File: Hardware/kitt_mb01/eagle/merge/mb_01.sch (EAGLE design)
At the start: 119 parts, among them IC1.01 RT8293A, IC2.00 BQ24266RGET, IC3.01 LSM9DS1, U0.1 SI1922EDH, U6.01 TPS61032RSARPSDO-G16, U7.01 SI1922EDH, U7.2 SI1922EDH, X2.01 S2B-PH-K-S(LF)(SN), X7.02 ARDUINO_UNO, X7.03 CON_HEADER_1X02, X7.05 MOTOR, X7.06 CON_HEADER_1X02, X7.08 CON_HEADER_1X02, X7.09 0R-JUMPA, X7.10 0R-JUMPA, X7.11 CON_HEADER_1X02

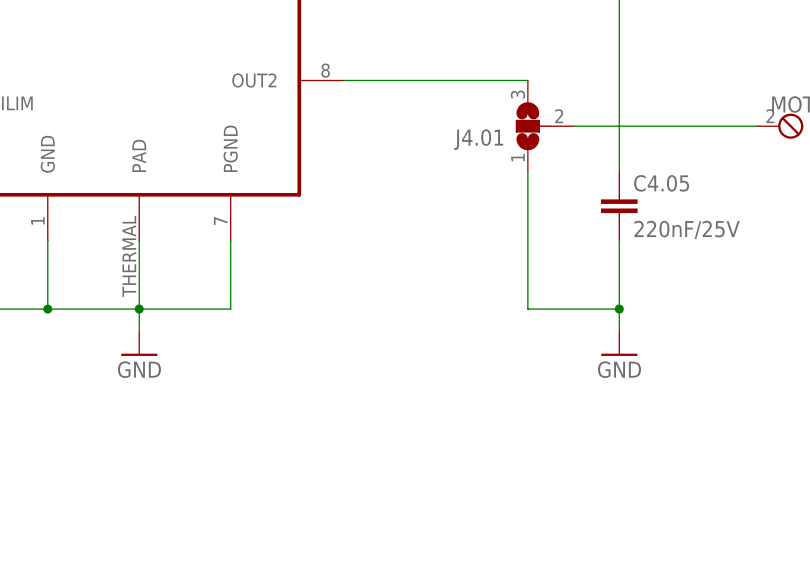
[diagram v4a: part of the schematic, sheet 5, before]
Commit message: updated bill of materials, changed some footprints
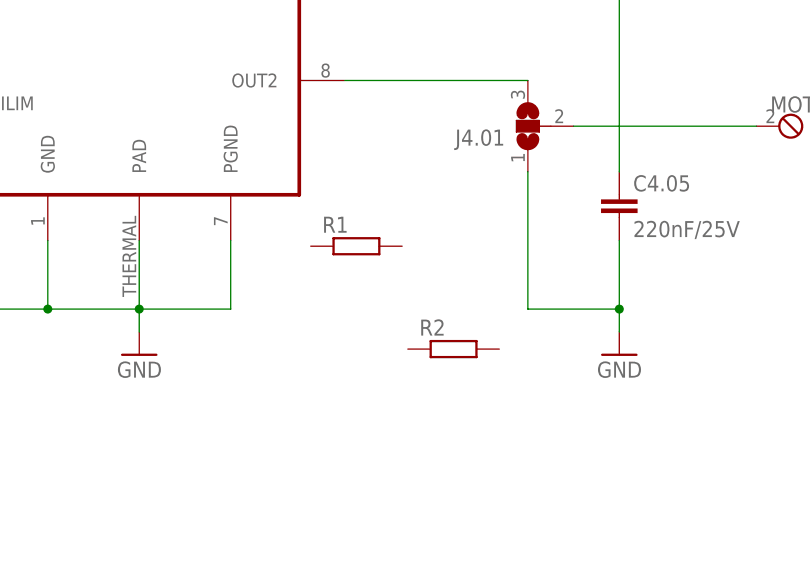
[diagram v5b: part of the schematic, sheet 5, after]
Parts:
- added R1: (no value), rcl:R-EU_R0805
- added R2: (no value), rcl:R-EU_R0402
- F1.01: device rcl:R-EU_R0805 -> rcl:R-EU_R1210
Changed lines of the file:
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@@
 <part name="P+6" library="supply1" deviceset="+12V" device="" value="V.POW"/>
 <part name="D1.01" library="diode" deviceset="MBRS3*0T3" device="" technology="2"/>
-<part name="F1.01" library="rcl" deviceset="R-EU_" device="R0805" value="750mA"/>
+<part name="F1.01" library="rcl" deviceset="R-EU_" device="R1210" value="750mA"/>
 <part name="L1.01" library="inductors" deviceset="BLM15H" device="" technology="B121SN1" value="BEAD"/>
 <part name="P+2" library="supply1" deviceset="+12V" device="" value="V.POW"/>
@@
 <part name="X7.03" library="kitt.con" deviceset="CON_HEADER_1X02" device=""/>
 <part name="R7.10" library="rcl" deviceset="R-EU_" device="R1206" value="330R"/>
+<part name="R1" library="rcl" deviceset="R-EU_" device="R0805"/>
+<part name="R2" library="rcl" deviceset="R-EU_" device="R0402"/>
 </parts>
 <sheets>
@@
 <instance part="R4.05" gate="G$1" x="99.06" y="73.66" rot="R90"/>
 <instance part="J4.01" gate="G$1" x="193.04" y="81.28" rot="R180"/>
+<instance part="R1" gate="G$1" x="173.99" y="67.945"/>
+<instance part="R2" gate="G$1" x="184.785" y="56.515"/>
 </instances>
 <busses>

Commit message: swapped footprint of LED resistors from 1206 to 0402
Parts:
- R7.04, R7.08, R7.09, R7.10: device rcl:R-EU_R1206 -> rcl:R-EU_R0603
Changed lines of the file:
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@@
 <part name="P+5VMAIN4" library="supply1" deviceset="+5V" device="" value="+5V-MAIN"/>
 <part name="U7.01" library="kitt.ic" deviceset="SI1922EDH" device=""/>
-<part name="R7.04" library="rcl" deviceset="R-EU_" device="R1206" value="330R"/>
+<part name="R7.04" library="rcl" deviceset="R-EU_" device="R0603" value="330R"/>
 <part name="GND33" library="supply1" deviceset="GND" device=""/>
 <part name="X7.10" library="jump-0r-smd" deviceset="0R-JUMP" device="A"/>
@@
 <part name="+3V10" library="supply1" deviceset="+3V3" device=""/>
 <part name="U7.2" library="kitt.ic" deviceset="SI1922EDH" device=""/>
-<part name="R7.09" library="rcl" deviceset="R-EU_" device="R1206" value="[0R]"/>
+<part name="R7.09" library="rcl" deviceset="R-EU_" device="R0603" value="[0R]"/>
 <part name="GND34" library="supply1" deviceset="GND" device=""/>
 <part name="X7.09" library="jump-0r-smd" deviceset="0R-JUMP" device="A"/>
@@
 <part name="X7.08" library="kitt.con" deviceset="CON_HEADER_1X02" device=""/>
 <part name="X7.11" library="kitt.con" deviceset="CON_HEADER_1X02" device=""/>
-<part name="R7.08" library="rcl" deviceset="R-EU_" device="R1206" value="330R"/>
+<part name="R7.08" library="rcl" deviceset="R-EU_" device="R0603" value="330R"/>
 <part name="GND12" library="supply1" deviceset="GND" device=""/>
 <part name="X7.06" library="kitt.con" deviceset="CON_HEADER_1X02" device=""/>
 <part name="X7.03" library="kitt.con" deviceset="CON_HEADER_1X02" device=""/>
-<part name="R7.10" library="rcl" deviceset="R-EU_" device="R1206" value="330R"/>
+<part name="R7.10" library="rcl" deviceset="R-EU_" device="R0603" value="330R"/>
 <part name="R1" library="rcl" deviceset="R-EU_" device="R0805"/>
 <part name="R2" library="rcl" deviceset="R-EU_" device="R0402"/>

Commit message: changed yet more footprints -> mainly the beads, stepped it up to a beefier part,    can handle 6A, should be better than the previous 1A rating
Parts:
- removed L1.01, L1.03, L4.01: BEAD, inductors:BLM15HB121SN1
- removed R1: (no value), rcl:R-EU_R0805
- removed R2: (no value), rcl:R-EU_R0402
- added FB1.01, FB1.02, FB4.01: BEAD, rcl:L-EUL4516C
- added L1: (no value), rcl:L-EUL1812
- added L2: (no value), rcl:L-EUL4516C
- C3.01: device rcl:C-EUC0402 -> rcl:C-EUC0603
- FB6.01: device inductors:BLM15HB121SN1 -> rcl:L-EUL4516C
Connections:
- net +12V: now also FB4.01.2; no longer L4.01.2
- net N$10: now also FB4.01.1; no longer L4.01.1
- net N$80: now also FB1.01.1; no longer L1.01.1
- net N$81: now also FB1.01.2; no longer L1.01.2
- net N$87: now also FB1.02.1; no longer L1.03.1
- net N$90: now also FB1.02.2; no longer L1.03.2
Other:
- moved on the sheet: FB6.01
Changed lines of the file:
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@@
 <part name="D1.01" library="diode" deviceset="MBRS3*0T3" device="" technology="2"/>
 <part name="F1.01" library="rcl" deviceset="R-EU_" device="R1210" value="750mA"/>
-<part name="L1.01" library="inductors" deviceset="BLM15H" device="" technology="B121SN1" value="BEAD"/>
+<part name="FB1.01" library="rcl" deviceset="L-EU" device="L4516C" value="BEAD"/>
 <part name="P+2" library="supply1" deviceset="+12V" device="" value="V.POW"/>
 <part name="C1.01" library="rcl" deviceset="C-EU" device="C1210K" value="22uF/25V"/>
@@
 <part name="L1.02" library="kitt.psvs" deviceset="NRS8030XX" device="" value="4.7uH"/>
 <part name="P+5VMAIN" library="supply1" deviceset="+5V" device="" value="+5V-MAIN"/>
-<part name="L1.03" library="inductors" deviceset="BLM15H" device="" technology="B121SN1" value="BEAD"/>
+<part name="FB1.02" library="rcl" deviceset="L-EU" device="L4516C" value="BEAD"/>
 <part name="FRAME1" library="frames" deviceset="A4L-LOC" device=""/>
 <part name="IC1.01" library="kitt.ic" deviceset="RT8293A" device=""/>
@@
 <part name="R3.08" library="rcl" deviceset="R-EU_" device="R0402" value="[10kR]"/>
 <part name="+3V3" library="supply1" deviceset="+3V3" device=""/>
-<part name="C3.01" library="rcl" deviceset="C-EU" device="C0402" value="10nF"/>
+<part name="C3.01" library="rcl" deviceset="C-EU" device="C0603" value="10nF"/>
 <part name="C3.02" library="rcl" deviceset="C-EU" device="C0402" value="100nF"/>
 <part name="C3.03" library="rcl" deviceset="C-EU" device="C0402" value="100nF"/>
@@
 <part name="C4.02" library="resistor" deviceset="C-EU" device="C0603K" value="100nF/25V"/>
 <part name="C4.03" library="resistor" deviceset="C-EU" device="C0805K"/>
-<part name="L4.01" library="inductors" deviceset="BLM15H" device="" technology="B121SN1" value="BEAD"/>
+<part name="FB4.01" library="rcl" deviceset="L-EU" device="L4516C" value="BEAD"/>
 <part name="GND21" library="supply1" deviceset="GND" device=""/>
 <part name="P+3" library="supply1" deviceset="+12V" device="" value="V.POW"/>
@@
 <part name="GND25" library="supply1" deviceset="GND" device=""/>
 <part name="P+5VMAIN3" library="supply1" deviceset="+5V" device="" value="+5V-MAIN"/>
-<part name="FB6.01" library="inductors" deviceset="BLM15H" device="" technology="B121SN1" value="BEAD"/>
+<part name="FB6.01" library="rcl" deviceset="L-EU" device="L4516C" value="BEAD"/>
 <part name="C6.04" library="kitt.psvs" deviceset="CPOL-2917" device="2312" value="100u"/>
 <part name="C6.05" library="kitt.psvs" deviceset="CPOL-2917" device="2312" value="100u"/>
@@
 <part name="X7.03" library="kitt.con" deviceset="CON_HEADER_1X02" device=""/>
 <part name="R7.10" library="rcl" deviceset="R-EU_" device="R0603" value="330R"/>
-<part name="R1" library="rcl" deviceset="R-EU_" device="R0805"/>
-<part name="R2" library="rcl" deviceset="R-EU_" device="R0402"/>
+<part name="L1" library="rcl" deviceset="L-EU" device="L1812"/>
+<part name="L2" library="rcl" deviceset="L-EU" device="L4516C"/>
 </parts>
 <sheets>
@@
 <instance part="D1.01" gate="G$1" x="31.75" y="106.68"/>
 <instance part="F1.01" gate="G$1" x="49.53" y="106.68"/>
-<instance part="L1.01" gate="G$1" x="62.23" y="106.68"/>
+<instance part="FB1.01" gate="G$1" x="62.23" y="106.68" rot="R90"/>
 <instance part="P+2" gate="1" x="41.91" y="114.3" smashed="yes">
 <attribute name="VALUE" x="39.37" y="114.3" size="1.778" layer="96" rot="R180"/>
@@
 <attribute name="VALUE" x="233.68" y="120.65" size="1.778" layer="96" rot="MR0"/>
 </instance>
-<instance part="L1.03" gate="G$1" x="222.25" y="99.06"/>
+<instance part="FB1.02" gate="G$1" x="222.25" y="99.06" rot="R90"/>
 <instance part="FRAME1" gate="G$1" x="0" y="0"/>
 <instance part="IC1.01" gate="G$1" x="123.19" y="96.52"/>
@@
 </instance>
 <instance part="GND29" gate="1" x="17.78" y="57.15"/>
+<instance part="L1" gate="G$1" x="167.64" y="118.11"/>
 </instances>
 <busses>
@@
 <segment>
 <pinref part="F1.01" gate="G$1" pin="2"/>
-<pinref part="L1.01" gate="G$1" pin="1"/>
+<pinref part="FB1.01" gate="G$1" pin="1"/>
 <wire x1="54.61" y1="106.68" x2="57.15" y2="106.68" width="0.1524" layer="91"/>
 </segment>
@@
 <segment>
 <pinref part="C1.01" gate="G$1" pin="1"/>
-<pinref part="L1.01" gate="G$1" pin="2"/>
+<pinref part="FB1.01" gate="G$1" pin="2"/>
 <wire x1="67.31" y1="81.28" x2="67.31" y2="106.68" width="0.1524" layer="91"/>
 <pinref part="IC1.01" gate="G$1" pin="VIN"/>
@@
 <wire x1="212.09" y1="99.06" x2="212.09" y2="83.82" width="0.1524" layer="91"/>
 <junction x="196.85" y="99.06"/>
-<pinref part="L1.03" gate="G$1" pin="1"/>
+<pinref part="FB1.02" gate="G$1" pin="1"/>
 <wire x1="217.17" y1="99.06" x2="212.09" y2="99.06" width="0.1524" layer="91"/>
 <junction x="212.09" y="99.06"/>
@@
 <net name="N$90" class="0">
 <segment>
-<pinref part="L1.03" gate="G$1" pin="2"/>
+<pinref part="FB1.02" gate="G$1" pin="2"/>
 <wire x1="227.33" y1="99.06" x2="229.87" y2="99.06" width="0.1524" layer="91"/>
 <pinref part="R1.05" gate="G$1" pin="2"/>
@@
 <instance part="C4.02" gate="G$1" x="68.58" y="121.92" rot="MR0"/>
 <instance part="C4.03" gate="G$1" x="48.26" y="121.92" rot="MR0"/>
-<instance part="L4.01" gate="G$1" x="58.42" y="129.54" rot="MR0"/>
+<instance part="FB4.01" gate="G$1" x="59.055" y="129.54" rot="MR90"/>
 <instance part="GND21" gate="1" x="48.26" y="106.68" rot="MR0"/>
 <instance part="P+3" gate="1" x="48.26" y="139.7" smashed="yes">
@@
 <instance part="R4.05" gate="G$1" x="99.06" y="73.66" rot="R90"/>
 <instance part="J4.01" gate="G$1" x="193.04" y="81.28" rot="R180"/>
-<instance part="R1" gate="G$1" x="173.99" y="67.945"/>
-<instance part="R2" gate="G$1" x="184.785" y="56.515"/>
+<instance part="L2" gate="G$1" x="218.44" y="62.23"/>
 </instances>
 <busses>
@@
 <wire x1="68.58" y1="129.54" x2="88.9" y2="129.54" width="0.1524" layer="91"/>
 <wire x1="88.9" y1="129.54" x2="88.9" y2="124.46" width="0.1524" layer="91"/>
-<pinref part="L4.01" gate="G$1" pin="1"/>
-<wire x1="68.58" y1="129.54" x2="63.5" y2="129.54" width="0.1524" layer="91"/>
+<pinref part="FB4.01" gate="G$1" pin="1"/>
+<wire x1="68.58" y1="129.54" x2="64.135" y2="129.54" width="0.1524" layer="91"/>
 <junction x="68.58" y="129.54"/>
 <wire x1="88.9" y1="129.54" x2="149.86" y2="129.54" width="0.1524" layer="91"/>
@@
 <pinref part="C4.03" gate="G$1" pin="1"/>
 <wire x1="48.26" y1="129.54" x2="48.26" y2="124.46" width="0.1524" layer="91"/>
-<pinref part="L4.01" gate="G$1" pin="2"/>
-<wire x1="53.34" y1="129.54" x2="48.26" y2="129.54" width="0.1524" layer="91"/>
+<pinref part="FB4.01" gate="G$1" pin="2"/>
+<wire x1="53.975" y1="129.54" x2="48.26" y2="129.54" width="0.1524" layer="91"/>
 <pinref part="P+3" gate="1" pin="+12V"/>
 <wire x1="48.26" y1="137.16" x2="48.26" y2="129.54" width="0.1524" layer="91"/>
@@
 <attribute name="VALUE" x="176.53" y="146.05" size="1.778" layer="96" rot="MR0"/>
 </instance>
-<instance part="FB6.01" gate="G$1" x="172.72" y="121.92" rot="R90"/>
+<instance part="FB6.01" gate="G$1" x="172.72" y="123.19" rot="R180"/>
 <instance part="C6.04" gate="G$1" x="172.72" y="109.22"/>
 <instance part="C6.05" gate="G$1" x="185.42" y="109.22"/>
@@
 <wire x1="172.72" y1="114.3" x2="172.72" y2="111.76" width="0.1524" layer="91"/>
 <pinref part="FB6.01" gate="G$1" pin="1"/>
-<wire x1="172.72" y1="114.3" x2="172.72" y2="116.84" width="0.1524" layer="91"/>
+<wire x1="172.72" y1="114.3" x2="172.72" y2="118.11" width="0.1524" layer="91"/>
 <pinref part="C6.04" gate="G$1" pin="+"/>
 <pinref part="C6.05" gate="G$1" pin="+"/>
@@
 <pinref part="R6.03" gate="G$1" pin="2"/>
 <pinref part="FB6.01" gate="G$1" pin="2"/>
-<wire x1="172.72" y1="129.54" x2="172.72" y2="127" width="0.1524" layer="91"/>
-</segment>
-</net>
+<wire x1="172.72" y1="129.54" x2="172.72" y2="128.27" width="0.1524" layer="91"/>
+</segment>
+</net>
